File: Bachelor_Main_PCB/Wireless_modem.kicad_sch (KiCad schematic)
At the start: 48 parts, among them J10 JAE_SIM_Card_SF72S006, J12 M20-9990245, Q1 SSM3J358R,LF, Q10 NX3008NBKW, Q11 NX3008NBKW, Q5 NX3008NBKW, Q6 NX3008NBKW, Q7 NX3008NBKW, Q8 NX3008NBKW, Q9 NX3008NBKW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

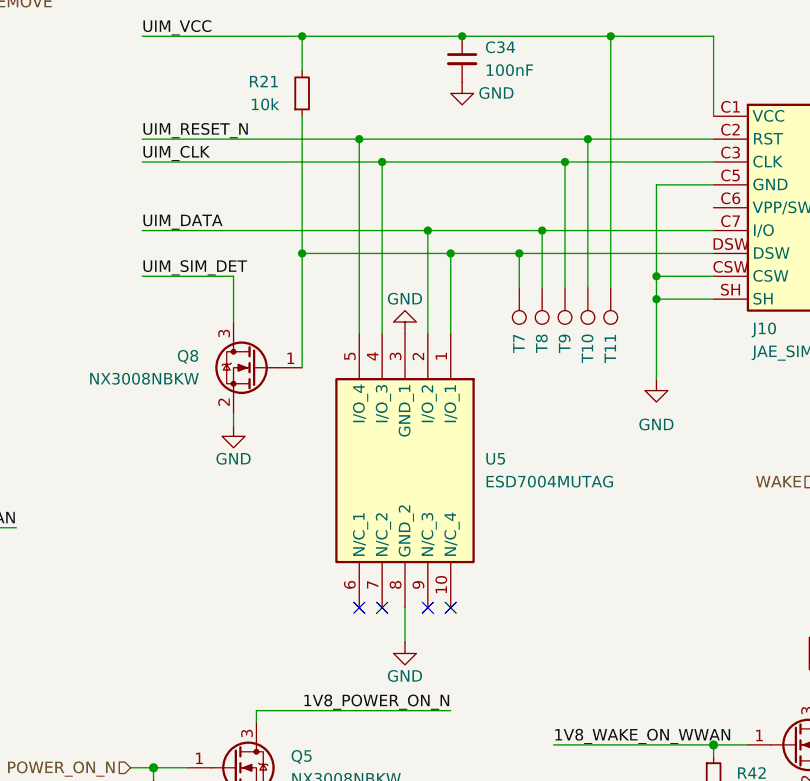
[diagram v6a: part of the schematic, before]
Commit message: Updated TVS diode routing through N/C pins
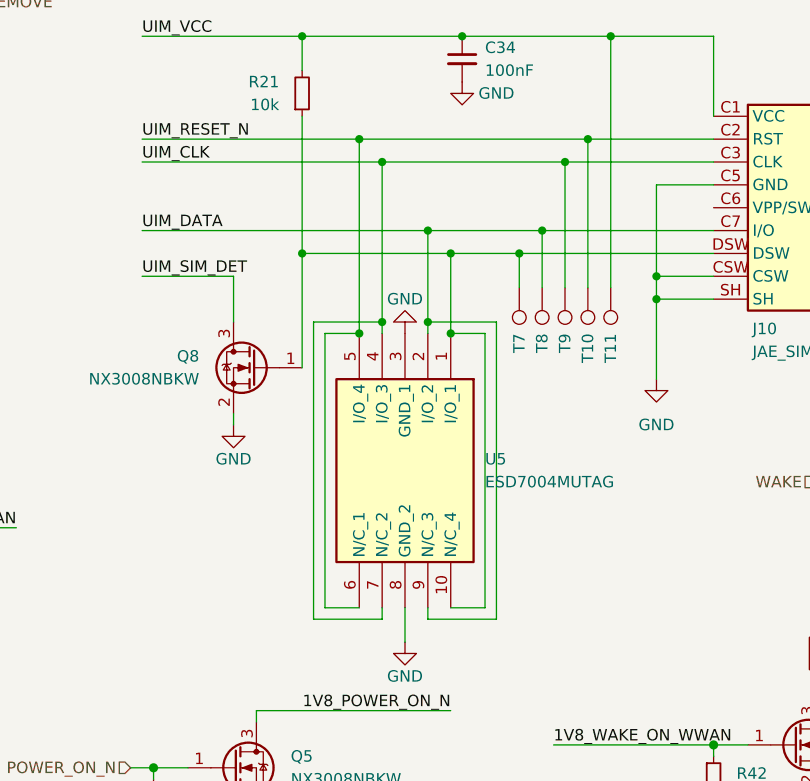
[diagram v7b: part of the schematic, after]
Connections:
- net UIM_CLK: now also U5.7 (N/C_2)
- net UIM_DATA: now also U5.9 (N/C_3)
- net UIM_RESET_N: now also U5.6 (N/C_1)
- net at J10.DSW, Q8.1 (G), R21.1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: now also U5.10 (N/C_4)
- no-connect marks 50 -> 46
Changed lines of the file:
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@@
+	)
+	(junction
+		(at 204.47 66.04)
+		(diameter 0)
+		(color 0 0 0 0)
 	)
 	(junction
@@
 	)
 	(junction
+		(at 212.09 64.77)
+		(diameter 0)
+		(color 0 0 0 0)
+	)
+	(junction
 		(at 198.12 33.02)
 		(diameter 0)
@@
 	)
 	(junction
+		(at 207.01 64.77)
+		(diameter 0)
+		(color 0 0 0 0)
+	)
+	(junction
 		(at 215.9 33.02)
 		(diameter 0)
@@
 	)
 	(junction
+		(at 214.63 66.04)
+		(diameter 0)
+		(color 0 0 0 0)
+	)
+	(junction
 		(at 128.27 176.53)
 		(diameter 0)
@@
 	)
 	(no_connect
-		(at 214.63 96.52)
-	)
-	(no_connect
 		(at 62.23 128.27)
 	)
@@
 	)
 	(no_connect
-		(at 204.47 96.52)
-	)
-	(no_connect
 		(at 143.51 54.61)
 	)
@@
 	)
 	(no_connect
-		(at 212.09 96.52)
-	)
-	(no_connect
 		(at 143.51 41.91)
 	)
 	(no_connect
-		(at 207.01 96.52)
-	)
-	(no_connect
 		(at 62.23 80.01)
 	)
@@
 	(wire
 		(pts
+			(xy 212.09 64.77) (xy 212.09 66.04)
+		)
+		(stroke
+			(width 0)
+			(type default)
+		)
+	)
+	(wire
+		(pts
+			(xy 200.66 96.52) (xy 200.66 66.04)
+		)
+		(stroke
+			(width 0)
+			(type default)
+		)
+	)
+	(wire
+		(pts
 			(xy 243.84 46.99) (xy 227.33 46.99)
 		)
@@
 	(wire
 		(pts
+			(xy 219.71 64.77) (xy 212.09 64.77)
+		)
+		(stroke
+			(width 0)
+			(type default)
+		)
+	)
+	(wire
+		(pts
 			(xy 29.21 154.94) (xy 29.21 152.4)
 		)
@@
 	(wire
 		(pts
+			(xy 214.63 96.52) (xy 218.44 96.52)
+		)
+		(stroke
+			(width 0)
+			(type default)
+		)
+	)
+	(wire
+		(pts
+			(xy 218.44 66.04) (xy 214.63 66.04)
+		)
+		(stroke
+			(width 0)
+			(type default)
+		)
+	)
+	(wire
+		(pts
 			(xy 237.49 62.23) (xy 243.84 62.23)
 		)
@@
 	(wire
 		(pts
-			(xy 212.09 54.61) (xy 212.09 66.04)
+			(xy 212.09 54.61) (xy 212.09 64.77)
 		)
 		(stroke
@@
 	(wire
 		(pts
-			(xy 207.01 46.99) (xy 207.01 66.04)
+			(xy 207.01 46.99) (xy 207.01 64.77)
 		)
 		(stroke
@@
 	(wire
 		(pts
+			(xy 218.44 96.52) (xy 218.44 66.04)
+		)
+		(stroke
+			(width 0)
+			(type default)
+		)
+	)
+	(wire
+		(pts
 			(xy 243.84 49.53) (xy 237.49 49.53)
 		)
@@
 	(wire
 		(pts
+			(xy 199.39 64.77) (xy 207.01 64.77)
+		)
+		(stroke
+			(width 0)
+			(type default)
+		)
+	)
+	(wire
+		(pts
 			(xy 41.91 29.21) (xy 62.23 29.21)
 		)
@@
 	(wire
 		(pts
+			(xy 199.39 97.79) (xy 199.39 64.77)
+		)
+		(stroke
+			(width 0)
+			(type default)
+		)
+	)
+	(wire
+		(pts
 			(xy 49.53 143.51) (xy 49.53 147.32)
 		)
@@
 	(wire
 		(pts
+			(xy 200.66 66.04) (xy 204.47 66.04)
+		)
+		(stroke
+			(width 0)
+			(type default)
+		)
+	)
+	(wire
+		(pts
 			(xy 193.04 107.95) (xy 193.04 109.22)
 		)
@@
 	(wire
 		(pts
+			(xy 207.01 97.79) (xy 199.39 97.79)
+		)
+		(stroke
+			(width 0)
+			(type default)
+		)
+	)
+	(wire
+		(pts
 			(xy 243.84 33.02) (xy 243.84 41.91)
 		)
@@
 	(wire
 		(pts
+			(xy 212.09 96.52) (xy 212.09 97.79)
+		)
+		(stroke
+			(width 0)
+			(type default)
+		)
+	)
+	(wire
+		(pts
 			(xy 212.09 54.61) (xy 224.79 54.61)
 		)
@@
 	(wire
 		(pts
+			(xy 212.09 97.79) (xy 219.71 97.79)
+		)
+		(stroke
+			(width 0)
+			(type default)
+		)
+	)
+	(wire
+		(pts
 			(xy 214.63 57.15) (xy 214.63 66.04)
 		)
@@
 	(wire
 		(pts
+			(xy 207.01 96.52) (xy 207.01 97.79)
+		)
+		(stroke
+			(width 0)
+			(type default)
+		)
+	)
+	(wire
+		(pts
 			(xy 215.9 33.02) (xy 232.41 33.02)
 		)
@@
 	(wire
 		(pts
+			(xy 207.01 64.77) (xy 207.01 66.04)
+		)
+		(stroke
+			(width 0)
+			(type default)
+		)
+	)
+	(wire
+		(pts
 			(xy 190.5 76.2) (xy 190.5 74.93)
 		)
@@
 	(wire
 		(pts
+			(xy 204.47 96.52) (xy 200.66 96.52)
+		)
+		(stroke
+			(width 0)
+			(type default)
+		)
+	)
+	(wire
+		(pts
 			(xy 190.5 59.69) (xy 190.5 64.77)
 		)
@@
 		)
 		(stroke
+			(width 0)
+			(type default)
+		)
+	)
+	(wire
+		(pts
+			(xy 219.71 97.79) (xy 219.71 64.77)
+		)
+		(stroke

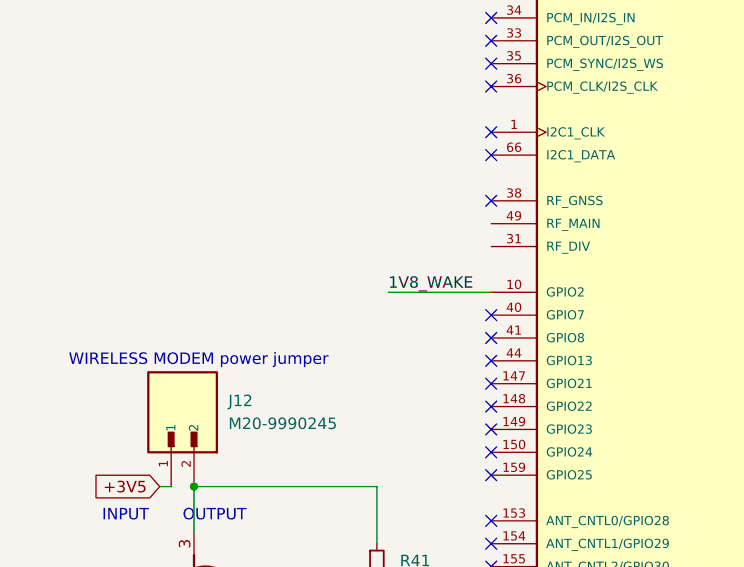
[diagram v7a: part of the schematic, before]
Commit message: MAIN_RF TVS diode and routed SDIO_DETECT
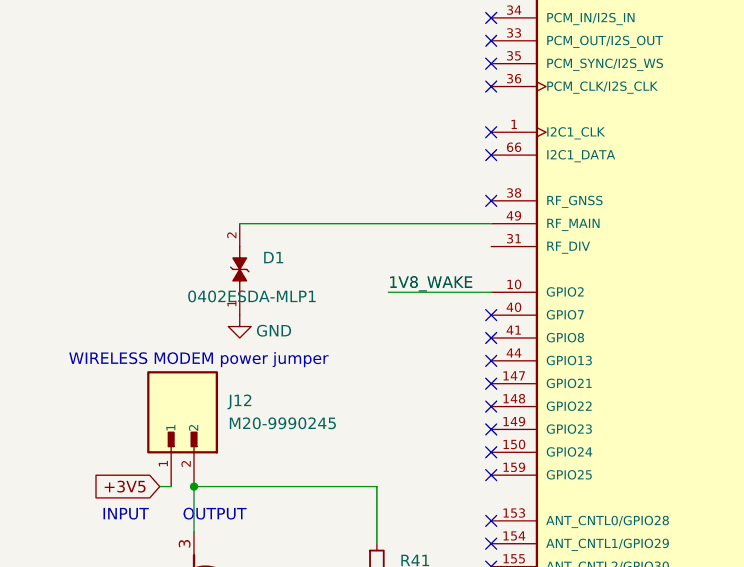
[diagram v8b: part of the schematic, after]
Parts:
- added D1: 0402ESDA-MLP1, 0402ESDA-MLP1:ESD_0402ESDA-MLP1, symbol 0402ESDA-MLP1:0402ESDA-MLP1
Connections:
- net GND: now also D1.1
- net at U2.49 (RF_MAIN): now also D1.2
